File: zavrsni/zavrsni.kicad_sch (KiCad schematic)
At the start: 62 parts, among them Q1 BC337, Q2 BC317, SW1 RotaryEncoder_Switch, SW2 SW_Push, SW3 SW_Push, SW4 SW_Push, SW5 SW_Push, SW6 SW_Push, SW7 SW_Push, SW8 SW_Push, SW9 SW_Push, U1 PCM3060, U2 WeAct STM32F411CEU6 v3.0, U3 NE5532, U4 TL074, U5 LM358, U6 LM317_TO-220, U7 UC1609C LCD Board

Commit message: PCB design, implement basic DAC/ADC
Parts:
- removed C12, C16, C3: 10u, Capacitor_THT:CP_Radial_D5.0mm_P2.50mm, symbol Device:C_Polarized_Small
- removed C17, C4: 100n, Capacitor_THT:C_Disc_D5.0mm_W2.5mm_P5.00mm, symbol Device:C_Small
- removed SW1: RotaryEncoder_Switch, Rotary_Encoder:RotaryEncoder_Alps_EC11E-Switch_Vertical_H20mm_CircularMountingHoles, symbol Device:RotaryEncoder_Switch
- removed SW3, SW4, SW5, SW6, SW7, SW8, SW9: SW_Push, Button_Switch_THT:SW_PUSH_6mm_H13mm, symbol Switch:SW_Push
- removed U1: PCM3060, Package_DIP:DIP-28_W15.24mm_Socket, symbol Audio:PCM3060
- added C12, C3: 100n, Capacitor_THT:C_Disc_D5.0mm_W2.5mm_P5.00mm, symbol Device:C_Small
- added C4: 10u, Capacitor_THT:CP_Radial_D5.0mm_P2.50mm, symbol Device:C_Polarized_Small
- added Jout1, Jvcc1, Jvss1: Conn_01x01_Pin, Connector_Wire:SolderWirePad_1x01_SMD_4x8mm, symbol Connector:Conn_01x01_Pin
- added SW1: EC11_SW, ljepi:ec11, symbol Device:RotaryEncoder_Switch_MP
- added SW_PRESET_1, SW_PRESET_2, SW_PRESET_3, SW_PRESET_4, SW_PRESET_5, SW_PRESET_6, SW_PRESET_7: SW_Push, Button_Switch_THT:SW_PUSH_6mm_H13mm, symbol Switch:SW_Push
- added U1: CS4335, Package_SO:SOIC-8_3.9x4.9mm_P1.27mm, symbol ljepe:CS4335
- Jin1: footprint Connector_Wire:SolderWirePad_1x01_SMD_3x6mm -> Connector_Wire:SolderWirePad_1x01_SMD_4x8mm
- renumbered SW2 to SW_PRESET_0
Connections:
- net +0V: now also Jvss1.1 (Pin_1)
- net +12V: now also C14.1, Jvcc1.1 (Pin_1)
- net +3V3: no longer C13.1, C14.2, R10.2
- net +5V: now also R10.2, U4.3 (+), C3.1, C4.1, U1.7 (VA); no longer C15.2, U4.10 (+)
- net GNDREF: now also C14.2, C15.2, U2.39 (GND), U4.10 (+), C12.2, C3.2, C4.2, SW1.C, SW1.MP, SW1.S2, SW_PRESET_1.2, SW_PRESET_2.2, SW_PRESET_3.2, SW_PRESET_4.2, SW_PRESET_5.2, SW_PRESET_6.2, SW_PRESET_7.2, U1.6 (AGND); no longer C14.1, C15.1, U4.5 (+)
- net at R10.1, R11.2: now also C15.1, U4.5 (+); no longer U4.3 (+)
- net LCD_VCC: now reaches U2.36 (B2), U7.4 (VDD)
- net LCD_VCC: now also C13.1, C12.1
- net LCD_SCK: now reaches U2.31 (A5), U7.5 (SCK)
- net LCD_SDA: now reaches U2.33 (A7), U7.6 (SDA)
- net LCD_RST: now reaches U2.32 (A6), U7.7 (RST)
- net LCD_CD: now reaches U2.35 (B1), U7.8 (CD)
- net LCD_CS: now reaches U2.34 (B0), U7.9 (CS)
- net at D1.2 (A), D2.1 (K), R9.1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: now also U4.2 (-); no longer U4.6 (-)
- net ADC_IN: now reaches U4.13 (-), U4.14
- net ADC_IN: now also U2.26 (A0)
- net at U4.7: now also R13.1, R9.2; no longer D1.1 (K)
- net at R12.1, R13.2: now also U4.6 (-); no longer U4.2 (-)
- net PRESET4: now reaches U2.12 (B4)
- net PRESET4: now also SW_PRESET_4.1
- net PRESET3: now reaches U2.13 (B5)
- net PRESET3: now also SW_PRESET_3.1
- net PRESET2: now reaches U2.14 (B6)
- net PRESET2: now also SW_PRESET_2.1
- net PRESET1: now reaches U2.15 (B7)
- net PRESET1: now also SW_PRESET_1.1
- net PRESET0: now reaches U2.17 (B9)
- net PRESET0: now also SW_PRESET_0.1
- net ROT_B: now reaches U2.2 (B13)
- net ROT_B: now also SW1.B
- net ROT_A: now reaches U2.3 (B14)
- net ROT_A: now also SW1.A
- net ROT_SW: now reaches U2.5 (A8)
- net ROT_SW: now also SW1.S1
- net PRESET7: now reaches U2.9 (A12)
- net PRESET7: now also SW_PRESET_7.1
- net at D2.2 (A): now also U4.1; no longer U4.8
- net PCM_ADC_DOUT renamed DAC_DAT
- net DAC_DAT: now also U1.1 (SDATA)
- net PCM_ADC_LR renamed DAC_LRCLK
- net DAC_LRCLK: now also U1.3 (LRCLK)
- net PCM_DAC_LR: no longer names the net of U2.30 (A4)
- net PCM_RST renamed DAC_MCLK
- net DAC_MCLK: now also U1.4 (MCLK)
- net PCM_SCKI renamed PRESET6
- net PRESET6: now also SW_PRESET_6.1
- net PCM_SCL renamed DAC_BCLK
- net DAC_BCLK: now also U1.2 (SCLK)
- net PCM_SDA renamed PRESET5
- net PRESET5: now also SW_PRESET_5.1
- new net: D1.1 (K), U4.8
- new net OUT: Jout1.1 (Pin_1), U1.5 (AOUTR)
- no-connect marks 5 -> 15
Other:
- note added: "Ograničavanje napona zvučnog signala između GND i VALG"
- note added: "Pojačavanje & pomicanje zvučnog signala za 1/2VALG"
- note added: "Strujni krug je dizajniran za napon napajanja od +12VDC. Napon napajanja može biti od +10VDC do +30VDC."
- note removed: "Ograničavanje napona zvučnog signala između 0V i Vcc"
- note removed: "Pojačavanje & pomicanje zvučnog signala za 1/2Vcc"
- moved on the sheet: C1, C18, C19, C2, C20, C7, D1, D2, H1, H2, H3, H4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

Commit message: PCB is done
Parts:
- removed SW1: EC11_SW, ljepi:ec11, symbol Device:RotaryEncoder_Switch_MP
- removed SW_PRESET_7: SW_Push, Button_Switch_THT:SW_PUSH_6mm_H13mm, symbol Switch:SW_Push
- U6: footprint Package_TO_SOT_THT:TO-220-3_Vertical -> Package_TO_SOT_THT:TO-220-3_Horizontal_TabDown
- renumbered SW_PRESET_5 to SW_DOWN1, SW_PRESET_6 to SW_OK1, SW_PRESET_4 to SW_UP1
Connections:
- net ROT_B is gone; now on net DAC_BCLK: U2.2 (B13)
- net +3V3: now also U2.38 (3V3)
- net DAC_BCLK: no longer U2.37 (B10)
- net PRESET0 renamed BTN_PRESET0
- net PRESET1 renamed BTN_PRESET1
- net PRESET2 renamed BTN_PRESET2
- net PRESET3 renamed BTN_PRESET3
- net PRESET4 renamed BTN_DOWN
- net BTN_DOWN: now also SW_DOWN1.1; no longer SW_UP1.1
- net PRESET5 renamed BTN_UP
- net BTN_UP: now also SW_UP1.1; no longer SW_DOWN1.1
- net PRESET6 renamed BTN_OK
- net PRESET7: no longer names the net of U2.9 (A12)
- net ROT_A: no longer names the net of U2.3 (B14)
- net ROT_SW: no longer names the net of U2.5 (A8)
- no-connect marks 15 -> 17

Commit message: PCB prototype finishing touches
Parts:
- removed R5: 1k, Resistor_THT:R_Axial_DIN0207_L6.3mm_D2.5mm_P10.16mm_Horizontal, symbol Device:R
- added RV1: R_Potentiometer_MountingPin, ljepi:pot vertikalni 5 pin, symbol Device:R_Potentiometer_MountingPin
- added SW_TUNER1: SW_Push, Button_Switch_THT:SW_PUSH_6mm_H13mm, symbol Switch:SW_Push
- C10, C23: now left out of the parts list
- D1, D2: footprint Diode_THT:D_DO-35_SOD27_P7.62mm_Horizontal -> Diode_THT:D_DO-35_SOD27_P2.54mm_Vertical_AnodeUp
- Q2: value BC317 -> BC327
- R1, R10, R12, R9: footprint Resistor_THT:R_Axial_DIN0207_L6.3mm_D2.5mm_P10.16mm_Horizontal -> Resistor_THT:R_Axial_DIN0207_L6.3mm_D2.5mm_P5.08mm_Vertical
- R11, R13, R2, R7, R8: footprint Resistor_THT:R_Axial_DIN0207_L6.3mm_D2.5mm_P10.16mm_Horizontal -> Resistor_THT:R_Axial_DIN0207_L6.3mm_D2.5mm_P2.54mm_Vertical
- R6: value 330 -> 300; footprint Resistor_THT:R_Axial_DIN0207_L6.3mm_D2.5mm_P10.16mm_Horizontal -> Resistor_THT:R_Axial_DIN0207_L6.3mm_D2.5mm_P2.54mm_Vertical
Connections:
- net +0V: now also Q2.1 (C); no longer Q2.3 (E)
- net BTN_DOWN: now also U2.11 (B3); no longer U2.12 (B4)
- net BTN_PRESET0: now also U2.15 (B7); no longer U2.17 (B9)
- net BTN_PRESET1: now also U2.14 (B6); no longer U2.15 (B7)
- net BTN_PRESET2: now also U2.13 (B5); no longer U2.14 (B6)
- net BTN_PRESET3: now also U2.12 (B4); no longer U2.13 (B5)
- net BTN_UP: now also U2.16 (B8); no longer U2.11 (B3)
- net GNDREF: now also Q2.3 (E), RV1.MP (MountPin), SW_TUNER1.2; no longer Q2.1 (C)
- net at R6.1, U3.6 (-): now also RV1.2
- net at C7.1, U3.7: now also RV1.1
- new net BTN_TUNER: SW_TUNER1.1, U2.17 (B9)
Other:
- moved on the sheet: C15, C7, D1, D2, R10, R11, R12, R13, R6, R9, U3B, U4A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

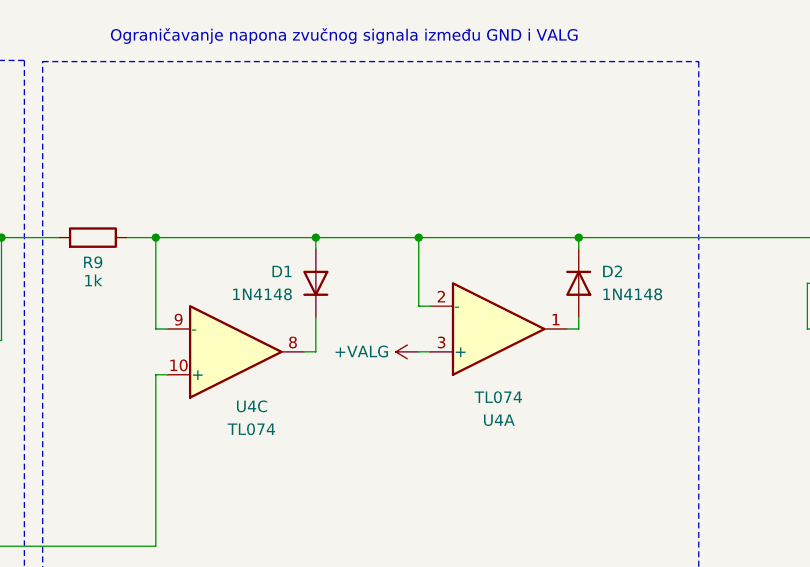
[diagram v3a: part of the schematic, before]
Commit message: izbrisi svg pdfove, zamjeni polaritet 2 diode
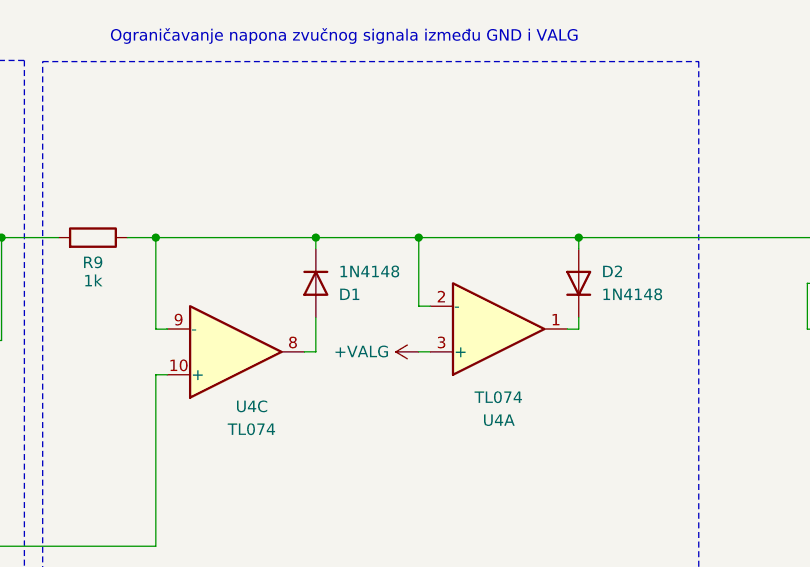
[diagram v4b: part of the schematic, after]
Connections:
- net at U4.1: now also D2.1 (K); no longer D2.2 (A)
- net at R9.1, U4.12 (+), U4.2 (-)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: now also D1.1 (K), D2.2 (A); no longer D1.2 (A), D2.1 (K)
- net at U4.8: now also D1.2 (A); no longer D1.1 (K)
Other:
- moved on the sheet: D1, D2
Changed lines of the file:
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@@
 	(symbol
 		(lib_id "Diode:1N4148")
-		(at 328.93 233.045 270)
+		(at 328.93 233.045 90)
 		(unit 1)
 		(exclude_from_sim no)
@@
 					(size 1.27 1.27)
 				)
-				(justify left)
+				(justify right)
 			)
 		)
@@
 					(size 1.27 1.27)
 				)
-				(justify left)
+				(justify right)
 			)
 		)
@@
 	(symbol
 		(lib_id "Diode:1N4148")
-		(at 299.72 233.045 270)
+		(at 299.72 233.045 90)
 		(mirror x)
 		(unit 1)
@@
 		(dnp no)
 		(property "Reference" "D1"
-			(at 297.18 231.7749 90)
+			(at 302.26 234.3151 90)
 			(effects
 				(font
@@
 		)
 		(property "Value" "1N4148"
-			(at 297.18 234.3149 90)
-			(effects
-				(font
+			(at 302.26 231.7751 90)
+			(effects
+				(font
